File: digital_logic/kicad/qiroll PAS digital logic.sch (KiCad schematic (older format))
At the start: 43 parts, among them J1 led_sw1, J2 mode_thr_batt, J3 pas_sense, J4 brk_sense, J5 jumper, U1 14538, U2 4023, U3 4027, U4 14538, U5 L7805, U6 4081, U7 4047, U8 74VHC1G32

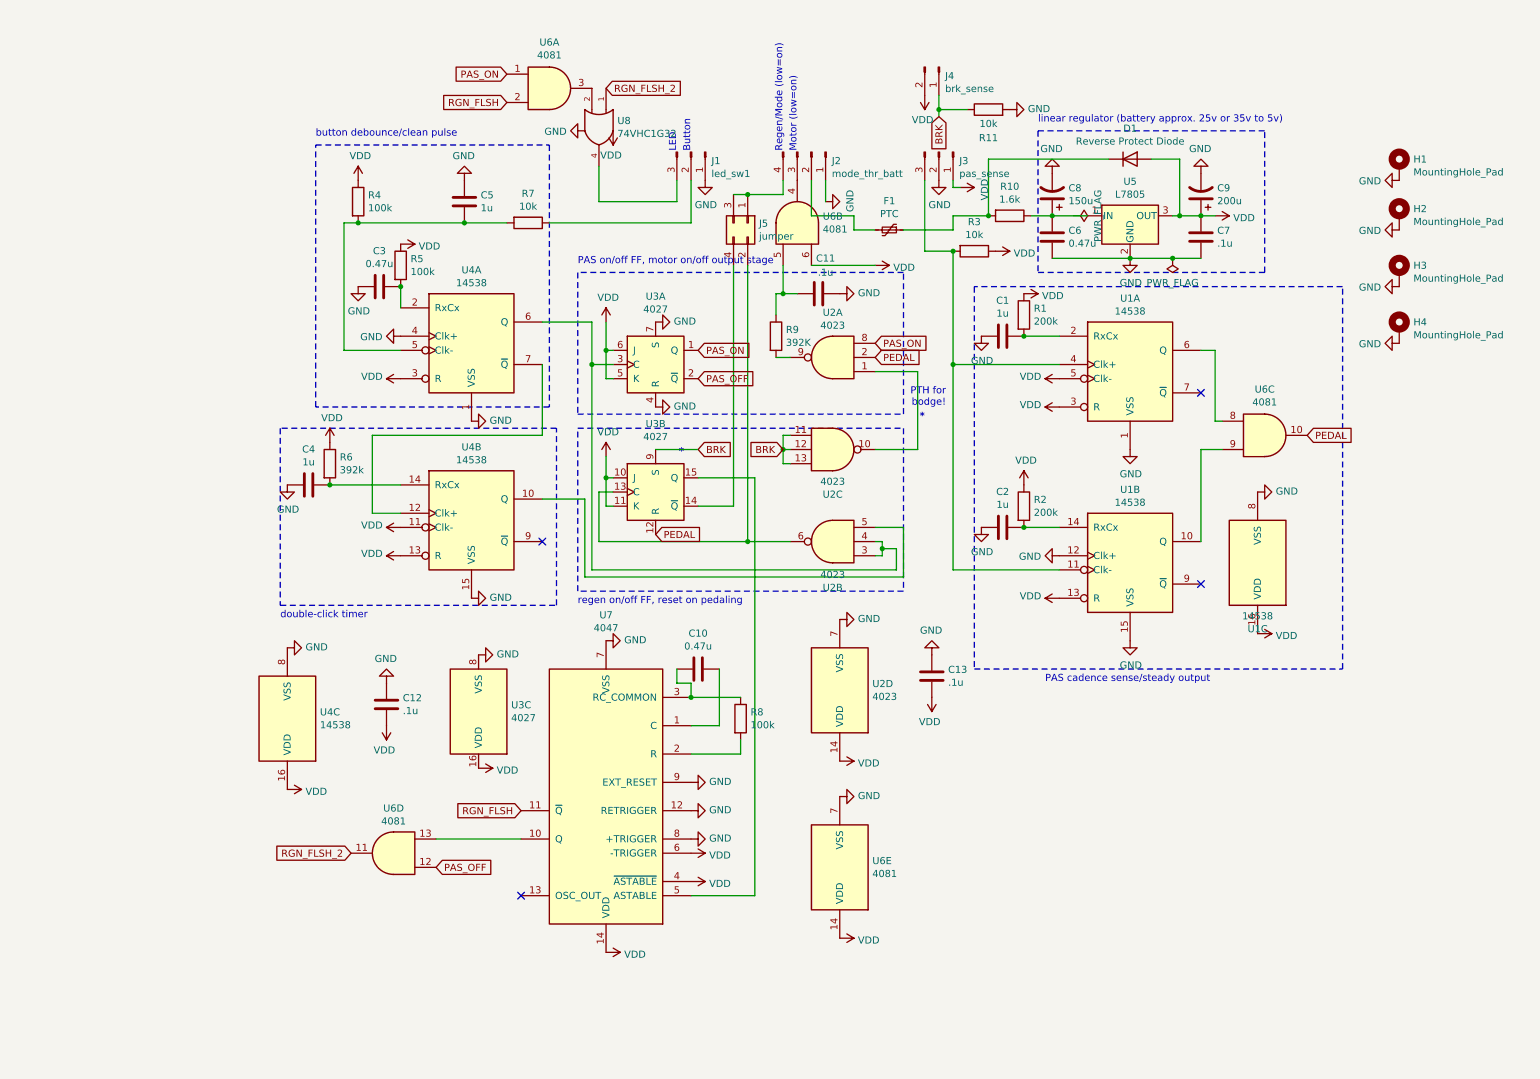
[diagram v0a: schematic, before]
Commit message: more Schmitt triggers\!
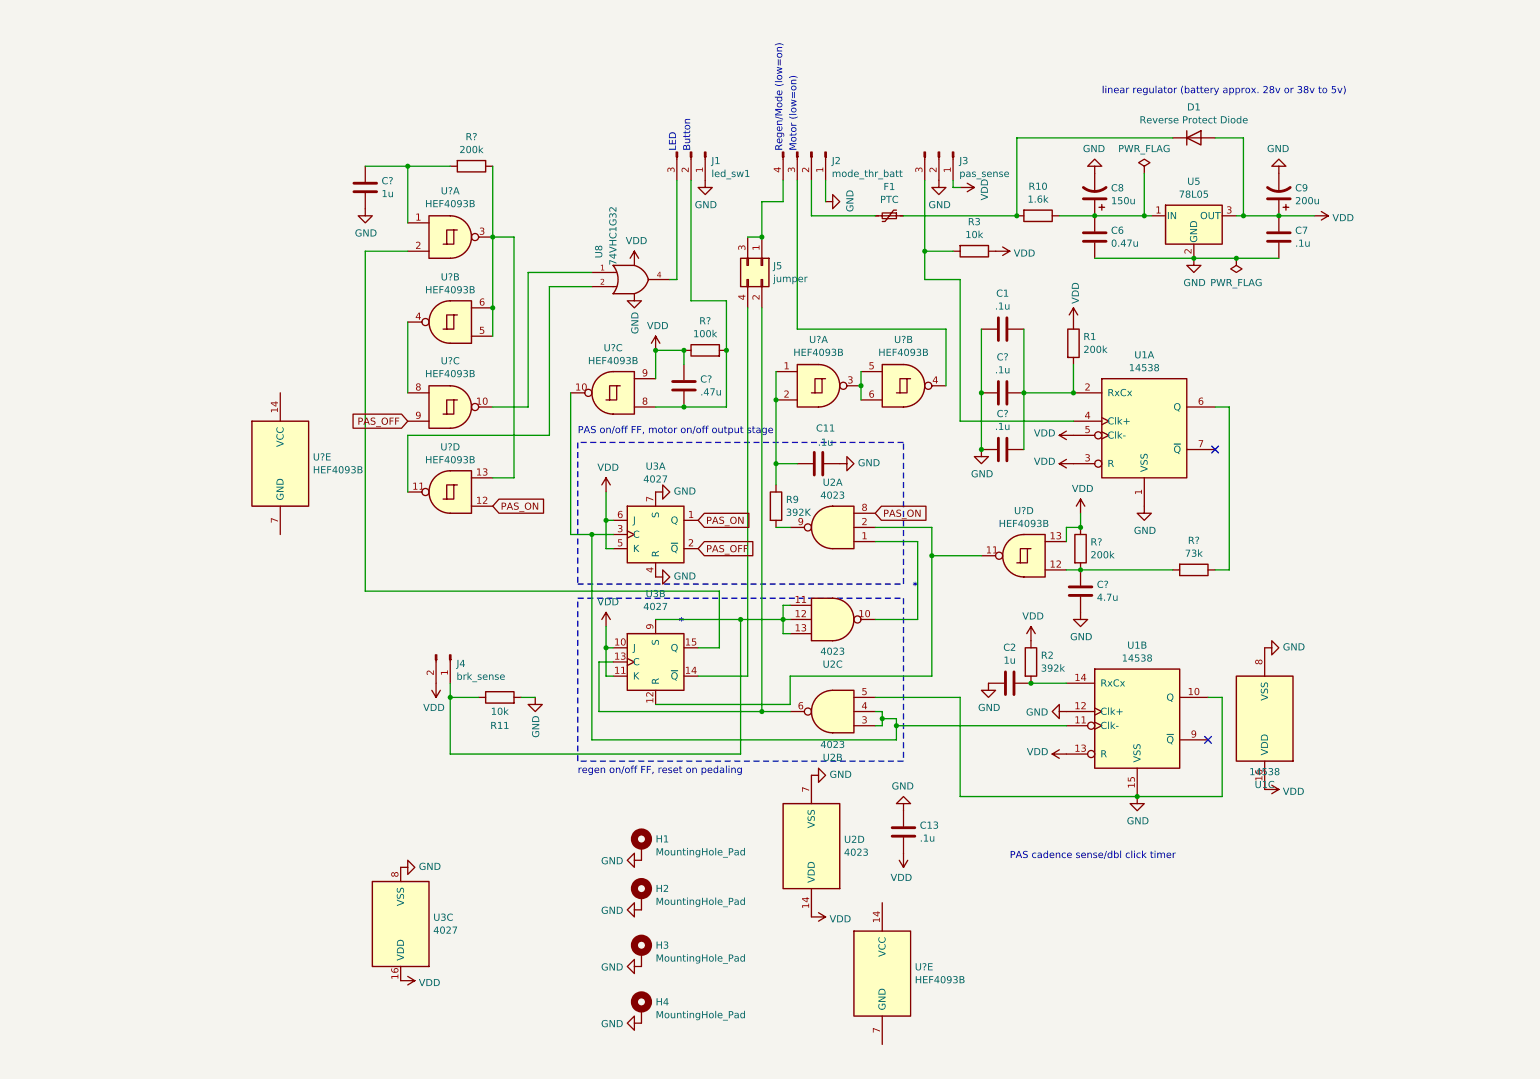
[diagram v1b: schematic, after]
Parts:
- removed C10, C3: 0.47u, Capacitor_SMD:C_0603_1608Metric, symbol Device:C
- removed C12: .1u, Capacitor_SMD:C_0603_1608Metric, symbol Device:C
- removed C4, C5: 1u, Capacitor_SMD:C_0603_1608Metric, symbol Device:C
- removed R4, R5, R8: 100k, Resistor_SMD:R_0603_1608Metric, symbol Device:R
- removed R6: 392k, Resistor_SMD:R_0603_1608Metric, symbol Device:R
- removed R7: 10k, Resistor_SMD:R_0603_1608Metric, symbol Device:R
- removed U4: 14538, Package_SO:SOIC-16_3.9x9.9mm_P1.27mm, symbol 4xxx:14538
- removed U6: 4081, Package_SO:SOIC-14_3.9x8.7mm_P1.27mm, symbol 4xxx:4081
- removed U7: 4047, Package_SO:SOIC-14_3.9x8.7mm_P1.27mm, symbol 4xxx:4047
- added C?: 1u, symbol Device:C
- added C? (x2): .1u, Capacitor_SMD:C_0603_1608Metric, symbol Device:C
- added C?: 4.7u, symbol Device:C
- added C?: .47u, symbol Device:C
- added R? (x2): 200k, symbol Device:R
- added R?: 73k, symbol Device:R
- added R?: 100k, symbol Device:R
- added U? (x10): HEF4093B, symbol 4xxx:HEF4093B
- C1: value 1u -> .1u
- R2: value 200k -> 392k
- U5: value L7805 -> 78L05
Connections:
- net GND: now also U1.10 (Q), U2.5, C?.2, C?.2, C?.2, C?.2
- net PAS_OFF: now also U?.9
- net PAS_ON: now also U?.12
- net VCC: now also C?.1, R?.1, R?.1, U?.13, U?.9
- net at C1.1, R1.2, U1.2 (RxCx): now also C?.1, C?.1
- net at J3.3 (Pin_3), R3.2, U1.4 (Clk+): no longer U1.11 (Clk-)
- net at U1.6 (Q): now also R?.1
- net at U2.3, U2.4, U3.3 (C): now also U1.11 (Clk-), U?.10
- net at U3.15 (Q): now also U?.2
- net at J1.2 (Pin_2): now also C?.2, R?.2, U?.8
- net at J2.3 (Pin_3): now also U?.4
- net at U8.2: now also U?.11
- net at C11.2, R9.1: now also U?.1, U?.2
- net BRK: no longer names the net of J4.1 (Pin_1), R11.1, U2.11, U2.12, U2.13, U3.9 (S)
- net PEDAL: no longer names the net of U2.2, U3.12 (R)
- net PEDAL: now also U?.11
- net RGN_FLSH_2: no longer names the net of U8.1
- net RGN_FLSH_2: now also U?.10
- new net: C?.1, R?.2, U?.1
- new net: R?.1, U?.13, U?.3, U?.5, U?.6
- new net: U?.4, U?.8
- new net: U?.3, U?.5, U?.6
- new net: C?.1, R?.2, R?.2, U?.12
- no-connect marks 4 -> 2
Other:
- note added: "PAS cadence sense/dbl click timer"
- note added: "linear regulator (battery approx. 28v or 38v to 5v)"
- note removed: "PAS cadence sense/steady output"
- note removed: "PTH for \nbodge!"
- note removed: "button debounce/clean pulse"
- note removed: "double-click timer"
- note removed: "linear regulator (battery approx. 25v or 35v to 5v)"
- moved on the sheet: C1, C11, C13, C2, C6, C7, C8, C9, D1, F1, H1, H2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

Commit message: trial component placement
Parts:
- removed C?: .1u, Capacitor_SMD:C_0603_1608Metric, symbol Device:C
- C1, C9: renamed from C?; footprint (none) -> Capacitor_SMD:C_0603_1608Metric
- C11: renamed from C6; value 0.47u -> .22u
- C2: renamed from C?; value .47u -> .22u; footprint (none) -> Capacitor_SMD:C_0603_1608Metric
- C6: renamed from C?; value .1u -> .22u
- D1: value Reverse Protect Diode -> LL4150GS18
- F1: value PTC -> 0ZCJ0012FF2E
- R1, R10, R9: renamed from R?; footprint (none) -> Resistor_SMD:R_0603_1608Metric
- R2: renamed from R11; value 10k -> 73k
- R3: renamed from R?; value 100k -> 200k; footprint (none) -> Resistor_SMD:R_0603_1608Metric
- R4: renamed from R9; value 392K -> 392k
- R5: renamed from R3; value 10k -> 73k
- U1, U3: renamed from U?; value HEF4093B -> CD4093B; footprint (none) -> Package_SO:SOIC-14_3.9x8.7mm_P1.27mm
- renumbered C8 to C10, C9 to C12, C7 to C13, C11 to C3, C13 to C4, C1 to C5, C2 to C8, J4 to J1, J1 to J2, J5 to J3, J2 to J4, J3 to J5, R2 to R6, R10 to R7, R1 to R8, U3 to U2, U8 to U4, U2 to U5, U1 to U6, U5 to U7
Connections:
- net GND: now also C4.2, U1.7 (GND), U3.7 (GND); no longer C4.1
- net VCC: now also C4.1, U1.14 (VCC), U3.14 (VCC); no longer C4.2
- net at U2.3 (C), U3.10, U6.11 (Clk-): no longer U5.3, U5.4
- net at J1.1 (Pin_1), R2.1, U2.9 (S)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: now also U5.3, U5.4
- net PAS_OFF: no longer names the net of U1.9, U2.2 (~Q)
- net PAS_ON: no longer names the net of U1.12, U2.1 (Q), U5.8
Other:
- moved on the sheet: C4, F1, H1, H2, H3, H4, R4, U1E, U2B, U2C, U3E, U5A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

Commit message: v2 PCB for review/manufacture
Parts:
- removed J3: jumper, Connector_PinHeader_2.54mm:PinHeader_2x02_P2.54mm_Vertical, symbol Connector_Generic:Conn_02x02_Odd_Even
- removed U4: 74VHC1G32, Package_SO:TSOP-5_1.65x3.05mm_P0.95mm, symbol 74xGxx:74AHC1G32
- removed U5: 4023, Package_SO:SOIC-14_3.9x8.7mm_P1.27mm, symbol 4xxx:4023
- removed U7: 78L05, Package_TO_SOT_THT:TO-92, symbol Regulator_Linear:L7805
- added J3, J6: Jumper, Connector_PinHeader_2.54mm:PinHeader_1x02_P2.54mm_Vertical, symbol Connector:Conn_01x02_Male
- added R11: 390k, Resistor_SMD:R_0603_1608Metric, symbol Device:R
- added U5: 4093B, Package_SO:SOIC-14_3.9x8.7mm_P1.27mm, symbol 4xxx:HEF4093B
- added U7: L78L05_TO92, Package_TO_SOT_THT:TO-92_Inline, symbol Regulator_Linear:L78L05_TO92
- R10, R2, R5: value 73k -> 75k
- R4, R6: value 392k -> 390k
- R8: value 200k -> 390k
- U1, U3: value CD4093B -> 4093B
- U2: value 4027 -> 4027B
- U6: value 14538 -> 14538B
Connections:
- net GND: now also C4.1, U5.7 (GND), U7.2 (GND); no longer C4.2, U6.10 (Q)
- net at U6.6 (Q): no longer R10.1
- net at U6.7 (~Q): now also R10.1
- net at U2.3 (C), U3.10, U6.11 (Clk-): now also U5.5
- net at U2.1 (Q): now also U1.9, U5.9; no longer U1.12
- net at U2.2 (~Q): now also U1.12; no longer U1.9
- net at U2.12 (R), U3.11: now also U5.8
- net at U2.13 (C): now also J3.1 (Pin_1), U5.4
- net at U2.14 (~Q): now also J6.2 (Pin_2)
- net at J1.1 (Pin_1), R2.1, U2.9 (S): now also U5.1, U5.2
- net at R4.2: now also U5.10
- net at C10.1, C11.1, R7.1: now also D1.1 (K), U7.3 (VI)
- net at J2.3 (Pin_3): now also U3.3
- net at J4.4 (Pin_4): now also J3.2 (Pin_2), J6.1 (Pin_1)
- net at C3.2, R4.1: now also U5.12, U5.13; no longer U3.1, U3.2
- net at F1.1, R7.2: no longer D1.1 (K)
- net at U1.10: now also U3.1
- net at U1.11: now also U3.2
- net at R1.1, U1.3, U1.5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: now also U1.8; no longer U1.13
- net at U1.4: now also U1.13; no longer U1.8
- net VCC renamed VDD
- net VDD: now also C4.2, U5.14 (VCC), U7.1 (VO); no longer C4.1
- new net: R11.2, U6.10 (Q)
- new net: U3.6, U5.3
- new net: R11.1, U5.6
- new net: U3.5, U5.11
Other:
- note added: "LED Behavior:\npedal assist on, regen off: solid on\npedal assist on, regen on: flashes\npedal assist off, regen off: off\npedal assist off, regen on: flashes"
- note added: "battery input PTC protection\n5v linear regulator (input max 20v or 33v after R7 drop)\nmin current approx. 3ma\nmax current approx. 5ma"
- note added: "battery power"
- note added: "brake"
- note added: "button"
- note added: "button debounce"
- note added: "connect J3 for std kit\nconnect J6 for pro kit"
- note added: "double-click"
- note added: "double-click timer\n"
- note added: "motor (low=on)"
- note added: "motor on/off logic\nsee note <<<"
- note added: "note: motor on/off logic\nmotor is on (output low)\nif not braking, pedal assist is on,\nand pedaling fast enough\notherwise, motor is off (output high)"
- note added: "note: pedal cadence sense\ncadence threshold is nominally\n45rpm on/32rpm off, \nwith C6 installed, C5 uninstalled,\nand typical 4093 Vp/Vn values\n\ninstall C5+C6 to lower threshold, or\nmake up for 4093 Vp/Vn variation\n\ninstall C5 only to raise threshold, or\nmake up for 4093 Vp/Vn variation\n"
- note added: "pedal"
- note added: "pedal assist on"
- note added: "pedal assist on/off FF, click toggles"
- note added: "pedal cadence sense\nsee note <<<"
- note added: "pedal sensor\n(square wave \n0-40hz)"
- note added: "regen braking/mode\n(low=on)"
- note added: "regen on/off FF, double-click toggles, \nreset on pedaling, set on braking"
- note added: "~brake"
- note removed: "*"
- note removed: "Button"
- note removed: "Motor (low=on)"
- note removed: "PAS cadence sense/dbl click timer"
- note removed: "PAS on/off FF, motor on/off output stage"
- note removed: "Regen/Mode (low=on)"
- note removed: "linear regulator (battery approx. 28v or 38v to 5v)"
- note removed: "regen on/off FF, reset on pedaling"
- moved on the sheet: C1, C10, C11, C12, C13, C2, C3, C4, C5, C6, C8, C9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

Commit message: v2 PCB for production
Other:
- note added: "note: pedal cadence sense\ncadence threshold is nominally\n40rpm on/29rpm off, \nwith C6 installed, C5 uninstalled,\nand typical 4093 Vp/Vn values\n(Vp = 3.3, Vn = 2.3)\n\ninstall C5+C6 to lower threshold, or\nmake up for 4093 Vp/Vn variation\n\ninstall C5 only to raise threshold, or\nmake up for 4093 Vp/Vn variation\n"
- note removed: "note: pedal cadence sense\ncadence threshold is nominally\n45rpm on/32rpm off, \nwith C6 installed, C5 uninstalled,\nand typical 4093 Vp/Vn values\n\ninstall C5+C6 to lower threshold, or\nmake up for 4093 Vp/Vn variation\n\ninstall C5 only to raise threshold, or\nmake up for 4093 Vp/Vn variation\n"
- moved on the sheet: R1, U1A, U1B
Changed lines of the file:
@@
 Date "2021-07-22"
 Rev "2"
-Comp "u/edibot42"
+Comp "Eric Dasmalchi"
 Comment1 ""
 Comment2 ""
@@
 L 4xxx:HEF4093B U1
 U 1 1 60F8A676
-P 2750 1900
-F 0 "U1" H 2750 2225 50  0000 C CNN
-F 1 "4093B" H 2750 2134 50  0000 C CNN
-F 2 "Package_SO:SOIC-14_3.9x8.7mm_P1.27mm" H 2750 1900 50  0001 C CNN
-F 3 "https://www.st.com/content/ccc/resource/technical/document/datasheet/63/6d/0c/9a/06/85/4d/aa/CD00000398.pdf/files/CD00000398.pdf/jcr:content/translations/en.CD00000398.pdf" H 2750 1900 50  0001 C CNN
-	1    2750 1900
+P 2900 1900
+F 0 "U1" H 2900 2225 50  0000 C CNN
+F 1 "4093B" H 2900 2134 50  0000 C CNN
+F 2 "Package_SO:SOIC-14_3.9x8.7mm_P1.27mm" H 2900 1900 50  0001 C CNN
+F 3 "https://www.st.com/content/ccc/resource/technical/document/datasheet/63/6d/0c/9a/06/85/4d/aa/CD00000398.pdf/files/CD00000398.pdf/jcr:content/translations/en.CD00000398.pdf" H 2900 1900 50  0001 C CNN
+	1    2900 1900
 	1    0    0    -1
 $EndComp
@@
 L 4xxx:HEF4093B U1
 U 2 1 60F9AADB
-P 2750 2500
-F 0 "U1" H 2750 2150 50  0000 C CNN
-F 1 "4093B" H 2750 2274 50  0000 C CNN
-F 2 "Package_SO:SOIC-14_3.9x8.7mm_P1.27mm" H 2750 2500 50  0001 C CNN
-F 3 "https://www.st.com/content/ccc/resource/technical/document/datasheet/63/6d/0c/9a/06/85/4d/aa/CD00000398.pdf/files/CD00000398.pdf/jcr:content/translations/en.CD00000398.pdf" H 2750 2500 50  0001 C CNN
-	2    2750 2500
+P 2900 2500
+F 0 "U1" H 2900 2150 50  0000 C CNN
+F 1 "4093B" H 2900 2274 50  0000 C CNN
+F 2 "Package_SO:SOIC-14_3.9x8.7mm_P1.27mm" H 2900 2500 50  0001 C CNN
+F 3 "https://www.st.com/content/ccc/resource/technical/document/datasheet/63/6d/0c/9a/06/85/4d/aa/CD00000398.pdf/files/CD00000398.pdf/jcr:content/translations/en.CD00000398.pdf" H 2900 2500 50  0001 C CNN
+	2    2900 2500
 	-1   0    0    1
 $EndComp
@@
 L Device:R R1
 U 1 1 60FAFC20
-P 2900 1400
-F 0 "R1" V 2693 1400 50  0000 C CNN
-F 1 "200k" V 2784 1400 50  0000 C CNN
-F 2 "Resistor_SMD:R_0603_1608Metric" V 2830 1400 50  0001 C CNN
-F 3 "https://www.digikey.com/en/products/detail/panasonic-electronic-components/ERJ-3GEYJ204V/104342" H 2900 1400 50  0001 C CNN
-	1    2900 1400
+P 3050 1400
+F 0 "R1" V 2843 1400 50  0000 C CNN
+F 1 "200k" V 2934 1400 50  0000 C CNN
+F 2 "Resistor_SMD:R_0603_1608Metric" V 2980 1400 50  0001 C CNN
+F 3 "https://www.digikey.com/en/products/detail/panasonic-electronic-components/ERJ-3GEYJ204V/104342" H 3050 1400 50  0001 C CNN
+	1    3050 1400
 	0    1    1    0
 $EndComp
@@
 	5350 5250 5500 5250
 Wire Wire Line
-	2150 1400 2450 1400
-Wire Wire Line
-	2450 1400 2450 1800
-Wire Wire Line
-	2450 1400 2750 1400
-Connection ~ 2450 1400
-Wire Wire Line
-	3050 1900 3050 1400
-Connection ~ 3050 1900
-Wire Wire Line
-	3050 1900 3050 2200
-Wire Wire Line
-	3050 2400 3050 2600
-Connection ~ 3050 2400
+	2150 1400 2600 1400
+Wire Wire Line
+	2600 1400 2600 1800
+Wire Wire Line
+	2600 1400 2900 1400
+Connection ~ 2600 1400
+Wire Wire Line
+	3200 1900 3200 1400
+Connection ~ 3200 1900
+Wire Wire Line
+	3200 1900 3200 2200
+Wire Wire Line
+	3200 2400 3200 2600
+Connection ~ 3200 2400
 $Comp
 L power:GND #PWR03
@@
 	5350 5450 5700 5450
 Wire Wire Line
-	2450 2000 2150 2000
+	2600 2000 2150 2000
 Wire Wire Line
 	2150 2000 2150 4800
@@
 	5600 3750 6900 3750
 Wire Wire Line
-	2350 2200 3050 2200
-Connection ~ 3050 2200
-Wire Wire Line
-	3050 2200 3050 2400
+	2350 2200 3200 2200
+Connection ~ 3200 2200
+Wire Wire Line
+	3200 2200 3200 2400
 $Comp
 L 4xxx:HEF4093B U5
@@
 note: motor on/off logic\nmotor is on (output low)\nif not braking, pedal assist is on,\nand pedaling fast enough\notherwise, motor is off (output high)
 Text Notes 500  3550 0    50   Italic 0
-note: pedal cadence sense\ncadence threshold is nominally\n45rpm on/32rpm off, \nwith C6 installed, C5 uninstalled,\nand typical 4093 Vp/Vn values\n\ninstall C5+C6 to lower threshold, or\nmake up for 4093 Vp/Vn variation\n\ninstall C5 only to raise threshold, or\nmake up for 4093 Vp/Vn variation\n
+note: pedal cadence sense\ncadence threshold is nominally\n40rpm on/29rpm off, \nwith C6 installed, C5 uninstalled,\nand typical 4093 Vp/Vn values\n(Vp = 3.3, Vn = 2.3)\n\ninstall C5+C6 to lower threshold, or\nmake up for 4093 Vp/Vn variation\n\ninstall C5 only to raise threshold, or\nmake up for 4093 Vp/Vn variation\n
 Wire Wire Line
 	3300 5950 5600 5950
@@
 Wire Wire Line
 	4550 3450 4550 3750
+Wire Wire Line
+	2450 2500 2600 2500
 $EndSCHEMATC
